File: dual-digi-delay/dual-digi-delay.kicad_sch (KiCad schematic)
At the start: 46 parts, among them J10 Delay Audio, J11 Delay2 Source, J12 Input Audio, J13 Delay1_CV, J14 Delay2_CV, J15 MidBoardPowerSend, J16 Delay Send, J17 Delay Return, J18 Delay Time Control, J19 LowerBoardPowerSend, J20 Main Power, J21 Delay Return, J22 Delay Send, J23 Delay Time Control, J24 MidBoardPowerRecv, J25 Delay Out, J26 Delay Audio, J27 Delay2_CV, J28 Output Audio, J29 Delay2 Source, J30 TopBoardPowerRecv, J31 Feedback Audio, J32 Input Audio, J33 Delay1_CV, J7 Output Audio, J8 Delay Out, J9 Feedback Audio

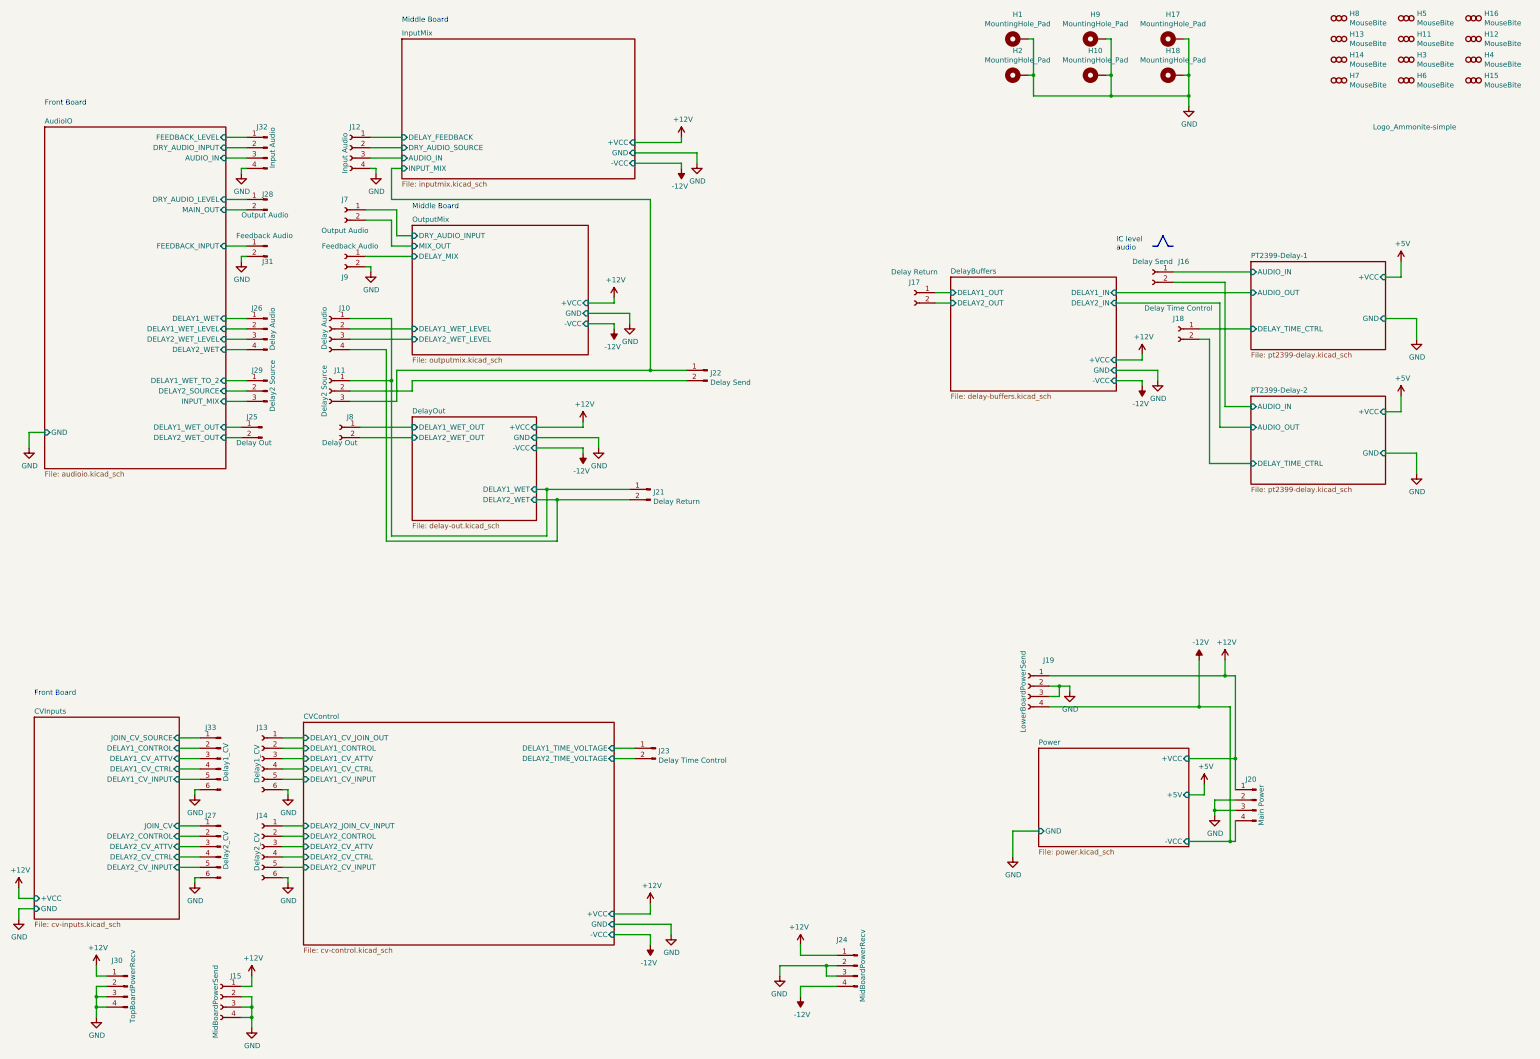
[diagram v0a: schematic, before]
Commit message: Making temporary branch for rev2 builds
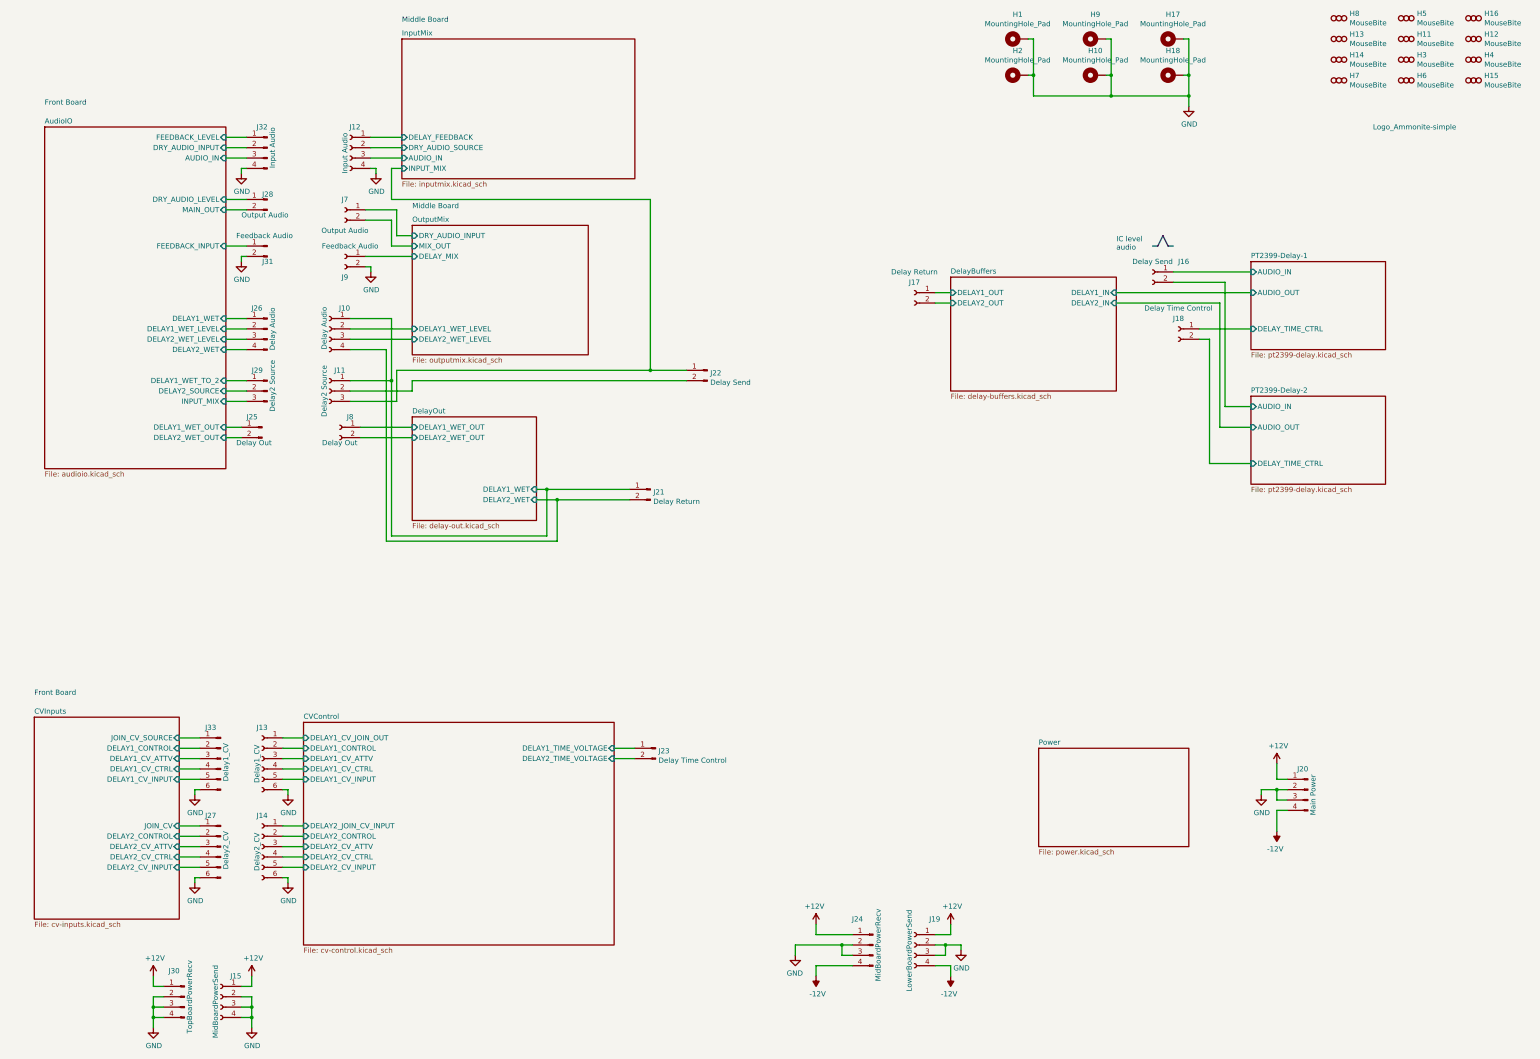
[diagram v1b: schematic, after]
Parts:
- H11, H12, H13, H14, H15, H16, H19, H3, H4, H5, H6, H7, H8: now left out of the parts list
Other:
- sheet AudioIO ports: added none; removed GND
- sheet CVControl ports: added none; removed +VCC, -VCC, GND
- sheet CVInputs ports: added none; removed +VCC, GND
- sheet DelayBuffers ports: added none; removed +VCC, -VCC, GND
- sheet DelayOut ports: added none; removed +VCC, -VCC, GND
- sheet InputMix ports: added none; removed +VCC, -VCC, GND
- sheet OutputMix ports: added none; removed +VCC, -VCC, GND
- sheet PT2399-Delay-1 ports: added none; removed +VCC, GND
- sheet PT2399-Delay-2 ports: added none; removed +VCC, GND
- sheet Power ports: added none; removed +5V, +VCC, -VCC, GND
- moved on the sheet: J19, J20, J24, J30
